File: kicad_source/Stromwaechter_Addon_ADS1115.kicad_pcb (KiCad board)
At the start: 2 copper layers, 84 x 21 mm, 23 parts, among them J1 SM04B-SRSS-TB, J2 SM04B-SRSS-TB, J3 MC_1,5_4-G-3.81, J4 MC_1,5_4-G-3.81, J5 MC_1,5_4-G-3.81, J6 MC_1,5_4-G-3.81, U1 ADS1115IDGS, U2 SRV05-4

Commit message: added some capacitors on vcc and a testpoint at ads1115_alert
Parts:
- added C10: 220 uF, Capacitor_SMD:CP_Elec_6.3x9.9, F.Cu at (205.0, 96.0)
- added C11: 220 uF, Capacitor_SMD:CP_Elec_6.3x9.9, F.Cu at (193.0, 96.0)
- added C6: 100 nF, Capacitor_SMD:C_0603_1608Metric, F.Cu at (141.0, 101.0)
- added C7: 100 nF, Capacitor_SMD:C_0603_1608Metric, F.Cu at (159.0, 101.0)
- added C8: 100 nF, Capacitor_SMD:C_0603_1608Metric, F.Cu at (178.0, 101.0)
- added C9: 100 nF, Capacitor_SMD:C_0603_1608Metric, F.Cu at (195.0, 101.0)
- added TP1: TestPoint, TestPoint:TestPoint_Pad_D1.5mm, F.Cu at (165.0, 99.0)
- moved C4 1.00 mm to (182.0, 101.0)
- moved R5 1.00 mm to (186.0, 101.0)
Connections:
- U1 pad 2: unconnected-(U1-ALERT/RDY-Pad2) -> /ADS1115_ALERT
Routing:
- net GND: track 138.9 -> 186.1 mm
- net +3.3V: track 127.0 -> 164.8 mm, vias 2 -> 3
- net /ADS1115_ALERT: track 0.00 -> 6.93 mm
- net /ADS1115_AIN2_R: track 16.7 -> 18.1 mm

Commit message: updated pcb
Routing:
- net /MP: track 13.6 -> 27.2 mm, vias 0 -> 4
- net +3.3V: track 164.8 -> 176.0 mm
- net GND: vias 5 -> 13
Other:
- board text added: "Stromwaechter_Addon_ADS1115 0.1 (c)2025"
- board text added: "bot"
- board text added: "top"

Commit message: added labels, made DRC
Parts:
- added FID1: Fiducial, generationmake:generationmake_small_solder, F.Cu at (210.3, 103.6)
- added FID2: Fiducial, generationmake:generationmake_logo, B.Cu at (175.0, 105.5)
- moved C5 1.00 mm to (198.0, 101.0)
- moved C9 1.00 mm to (194.0, 101.0)
- moved R6 1.00 mm to (202.0, 101.0)
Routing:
- net GND: track 186.1 -> 187.1 mm
- net /ADS1115_AIN3_R: track 36.3 -> 35.3 mm
- net /ADS1115_AIN2_R: track 18.1 -> 17.1 mm

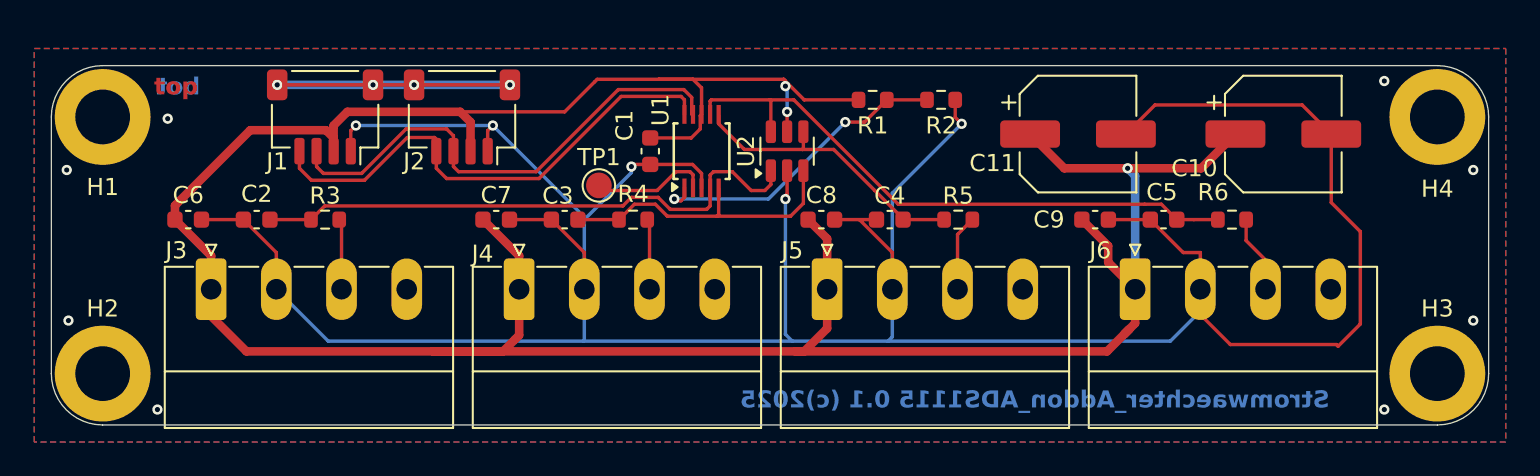
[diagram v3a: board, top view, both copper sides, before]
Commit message: fixed DRC errors
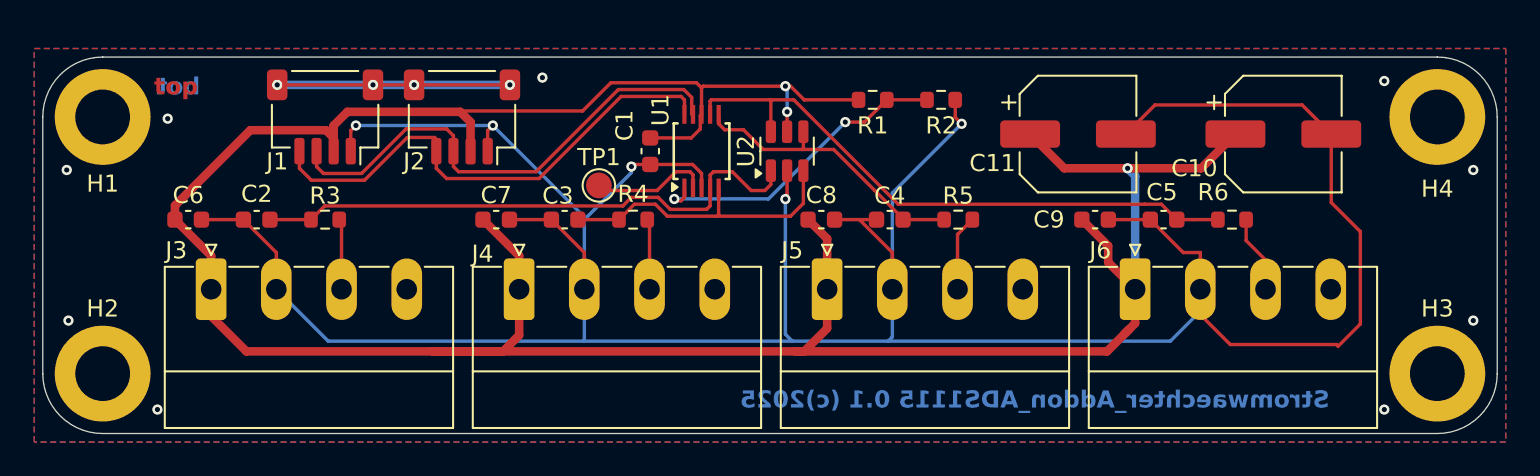
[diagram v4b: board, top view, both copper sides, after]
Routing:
- net +3.3V: track 176.0 -> 171.3 mm
- net GND: vias 13 -> 14
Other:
- board size 84 x 21 mm -> 85 x 22 mm
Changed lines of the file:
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@@
 		(tags "mounting hole 3.2mm m3 din965")
 		(property "Reference" "H1"
-			(at 0 4.1 0)
+			(at 0 3.9 0)
 			(layer "F.SilkS")
 			(effects
@@
 	)
 	(gr_arc
-		(start 217 110)
-		(mid 216.12132 112.12132)
-		(end 214 113)
+		(start 217.5 110)
+		(mid 216.474874 112.474874)
+		(end 214 113.5)
 		(stroke
 			(width 0.05)
@@
 	)
 	(gr_arc
-		(start 133 95)
-		(mid 133.87868 92.87868)
-		(end 136 92)
+		(start 132.5 95)
+		(mid 133.525126 92.525126)
+		(end 136 91.5)
 		(stroke
 			(width 0.05)
@@
 	)
 	(gr_line
-		(start 136 92)
-		(end 214 92)
+		(start 136 91.5)
+		(end 214 91.5)
 		(stroke
 			(width 0.05)
@@
 	)
 	(gr_line
-		(start 133 110)
-		(end 133 95)
+		(start 132.5 110)
+		(end 132.5 95)
 		(stroke
 			(width 0.05)
@@
 	)
 	(gr_arc
-		(start 136 113)
-		(mid 133.87868 112.12132)
-		(end 133 110)
+		(start 136 113.5)
+		(mid 133.525126 112.474874)
+		(end 132.5 110)
 		(stroke
 			(width 0.05)
@@
 	)
 	(gr_line
-		(start 214 113)
-		(end 136 113)
+		(start 214 113.5)
+		(end 136 113.5)
 		(stroke
 			(width 0.05)
@@
 	)
 	(gr_arc
-		(start 214 92)
-		(mid 216.12132 92.87868)
-		(end 217 95)
+		(start 214 91.5)
+		(mid 216.474874 92.525126)
+		(end 217.5 95)
 		(stroke
 			(width 0.05)
@@
 	)
 	(gr_line
-		(start 217 95)
-		(end 217 110)
+		(start 217.5 95)
+		(end 217.5 110)
 		(stroke
 			(width 0.05)
@@
 	)
 	(segment
-		(start 168.5 92.8)
-		(end 175.8 92.8)
+		(start 164.05 94.65)
+		(end 156.95 94.65)
+		(width 0.2)
+		(layer "F.Cu")
+		(net 1)
+	)
+	(segment
+		(start 170.7 93)
+		(end 165.7 93)
 		(width 0.2)
 		(layer "F.Cu")
@@
 	)
 	(segment
-		(start 195.7 107.7)
-		(end 196 107.4)
-		(width 0.5)
+		(start 171.1 93.2)
+		(end 171 93.3)
+		(width 0.2)
 		(layer "F.Cu")
 		(net 1)
 	)
 	(segment
-		(start 170.5 92.8)
-		(end 168.5 92.8)
-		(width 0.2)
+		(start 195.7 107.7)
+		(end 196 107.4)
+		(width 0.5)
 		(layer "F.Cu")
 		(net 1)
@@
 	)
 	(segment
-		(start 168.5 92.8)
-		(end 164.9 92.8)
-		(width 0.2)
+		(start 160.34 103.115)
+		(end 158.225 101)
+		(width 0.5)
 		(layer "F.Cu")
 		(net 1)
 	)
 	(segment
-		(start 160.34 103.115)
-		(end 158.225 101)
-		(width 0.5)
+		(start 177 94)
+		(end 176.2 93.2)
+		(width 0.2)
 		(layer "F.Cu")
 		(net 1)
@@
 	)
 	(segment
+		(start 176.2 93.2)
+		(end 175.9 93.2)
+		(width 0.2)
+		(layer "F.Cu")
+		(net 1)
+	)
+	(segment
 		(start 160.34 105.0675)
 		(end 160.34 103.115)
@@
 	)
 	(segment
-		(start 164.9 92.8)
-		(end 164.75 92.95)
-		(width 0.2)
-		(layer "F.Cu")
-		(net 1)
-	)
-	(segment
 		(start 194.7625 102.5375)
 		(end 194.7625 103.49)
@@
 	)
 	(segment
-		(start 175.9 92.9)
-		(end 175.8 92.8)
-		(width 0.2)
-		(layer "F.Cu")
-		(net 1)
-	)
-	(segment
 		(start 178.34 102.115)
 		(end 177.225 101)
@@
 	)
 	(segment
-		(start 177 108.7)
-		(end 178.34 107.36)
-		(width 0.5)
-		(layer "F.Cu")
-		(net 1)
-	)
-	(segment
-		(start 156.2 94.7)
-		(end 163 94.7)
+		(start 175.9 93.2)
+		(end 171.1 93.2)
 		(width 0.2)
 		(layer "F.Cu")
@@
 	)
 	(segment
-		(start 163 94.7)
-		(end 164.75 92.95)
-		(width 0.2)
+		(start 177 108.7)
+		(end 178.34 107.36)
+		(width 0.5)
 		(layer "F.Cu")
 		(net 1)
@@
 	)
 	(segment
-		(start 177 94)
-		(end 175.8 92.8)
-		(width 0.2)
-		(layer "F.Cu")
-		(net 1)
-	)
-	(segment
-		(start 175.9 93.2)
-		(end 175.9 92.9)
-		(width 0.2)
-		(layer "F.Cu")
-		(net 1)
-	)
-	(segment
 		(start 142.34 106.64)
 		(end 144.4 108.7)
@@
 	)
 	(segment
+		(start 171 93.3)
+		(end 170.7 93)
+		(width 0.2)
+		(layer "F.Cu")
+		(net 1)
+	)
+	(segment
 		(start 142.34 106.64)
 		(end 142.34 105.0675)
@@
 	)
 	(segment
-		(start 156.2 94.7)
+		(start 156.95 94.65)
 		(end 156.9 94.7)
 		(width 0.2)
@@
 	)
 	(segment
-		(start 170.5 92.8)
-		(end 171 93.3)
+		(start 165.7 93)
+		(end 164.05 94.65)
 		(width 0.2)
 		(layer "F.Cu")
@@
 	)
 	(via
+		(at 161.7 92.7)
+		(size 0.6)
+		(drill 0.3)
+		(layers "F.Cu" "B.Cu")
+		(free yes)
+		(net 2)
+	)
+	(via
 		(at 166.9 97.9)
 		(size 0.6)
@@
 	)
 	(segment
+		(start 176.9 96.9)
+		(end 174.6 96.9)
+		(width 0.2)
+		(layer "F.Cu")
+		(net 5)
+	)
+	(segment
 		(start 172 95.4)
 		(end 172 94.85)
@@
 	)
 	(segment
-		(start 176.95 95.8625)
-		(end 176.95 96.85)
+		(start 172.35 95.75)
+		(end 172 95.4)
 		(width 0.2)
 		(layer "F.Cu")
@@
 	)
 	(segment
-		(start 173.5 96.9)
-		(end 172 95.4)
+		(start 176.95 95.8625)
+		(end 176.95 96.85)
 		(width 0.2)
 		(layer "F.Cu")
@@
 	)
 	(segment
-		(start 176.9 96.9)
-		(end 173.5 96.9)
+		(start 173.45 95.75)
+		(end 172.35 95.75)
+		(width 0.2)
+		(layer "F.Cu")
+		(net 5)
+	)
+	(segment
+		(start 174.6 96.9)
+		(end 173.45 95.75)
 		(width 0.2)
 		(layer "F.Cu")
